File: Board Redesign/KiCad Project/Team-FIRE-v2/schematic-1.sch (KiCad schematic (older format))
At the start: 20 parts

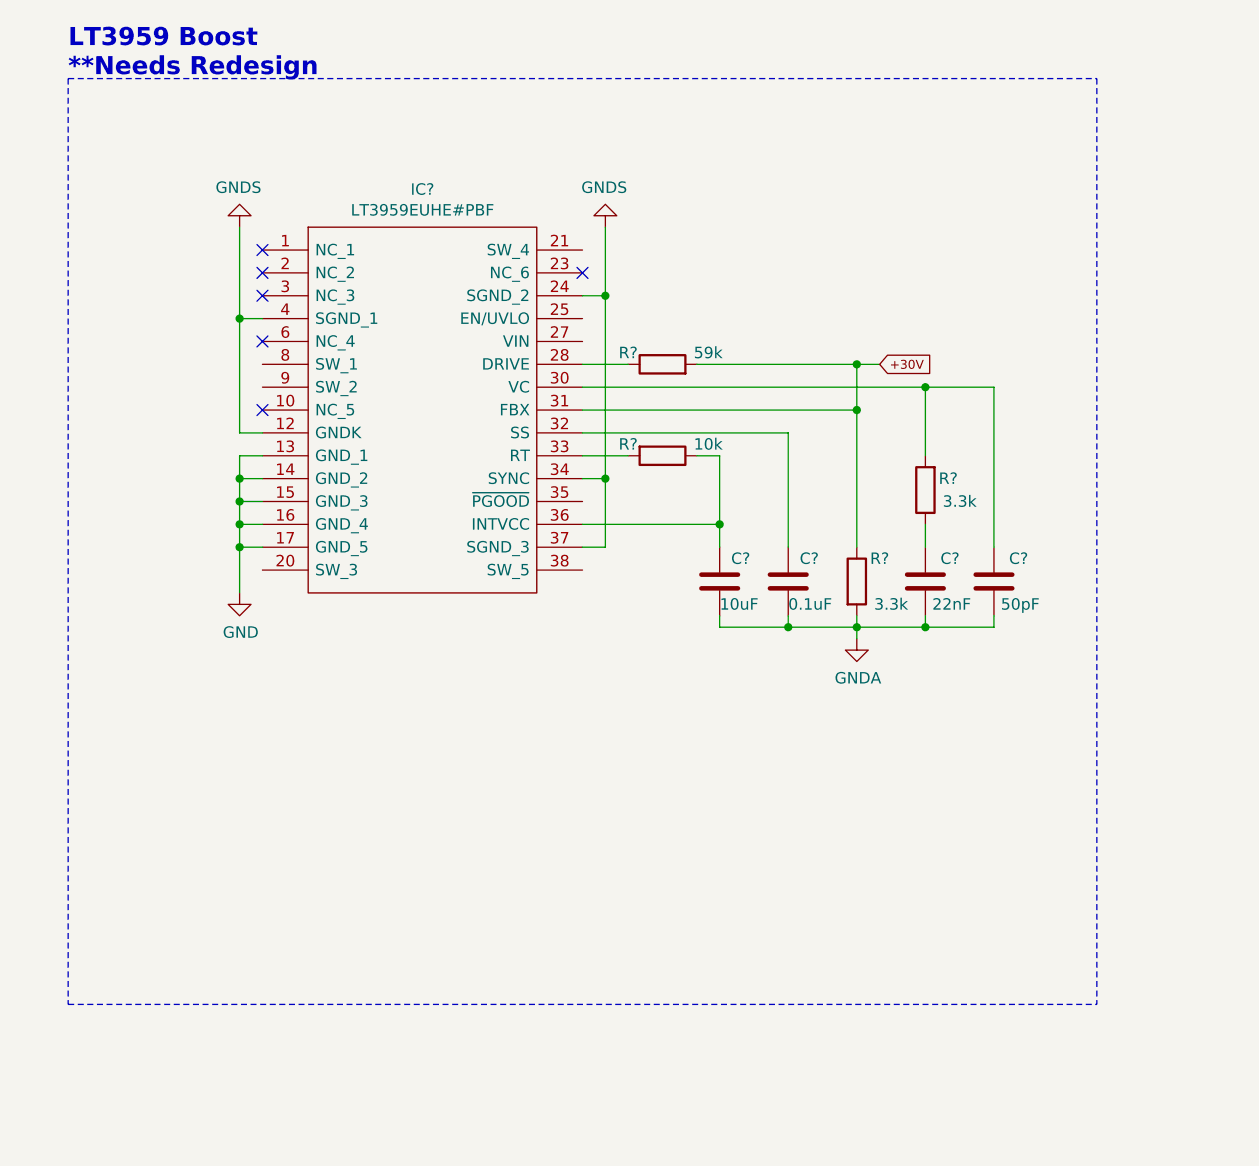
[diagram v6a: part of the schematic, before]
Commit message: Deleted Old Boost...
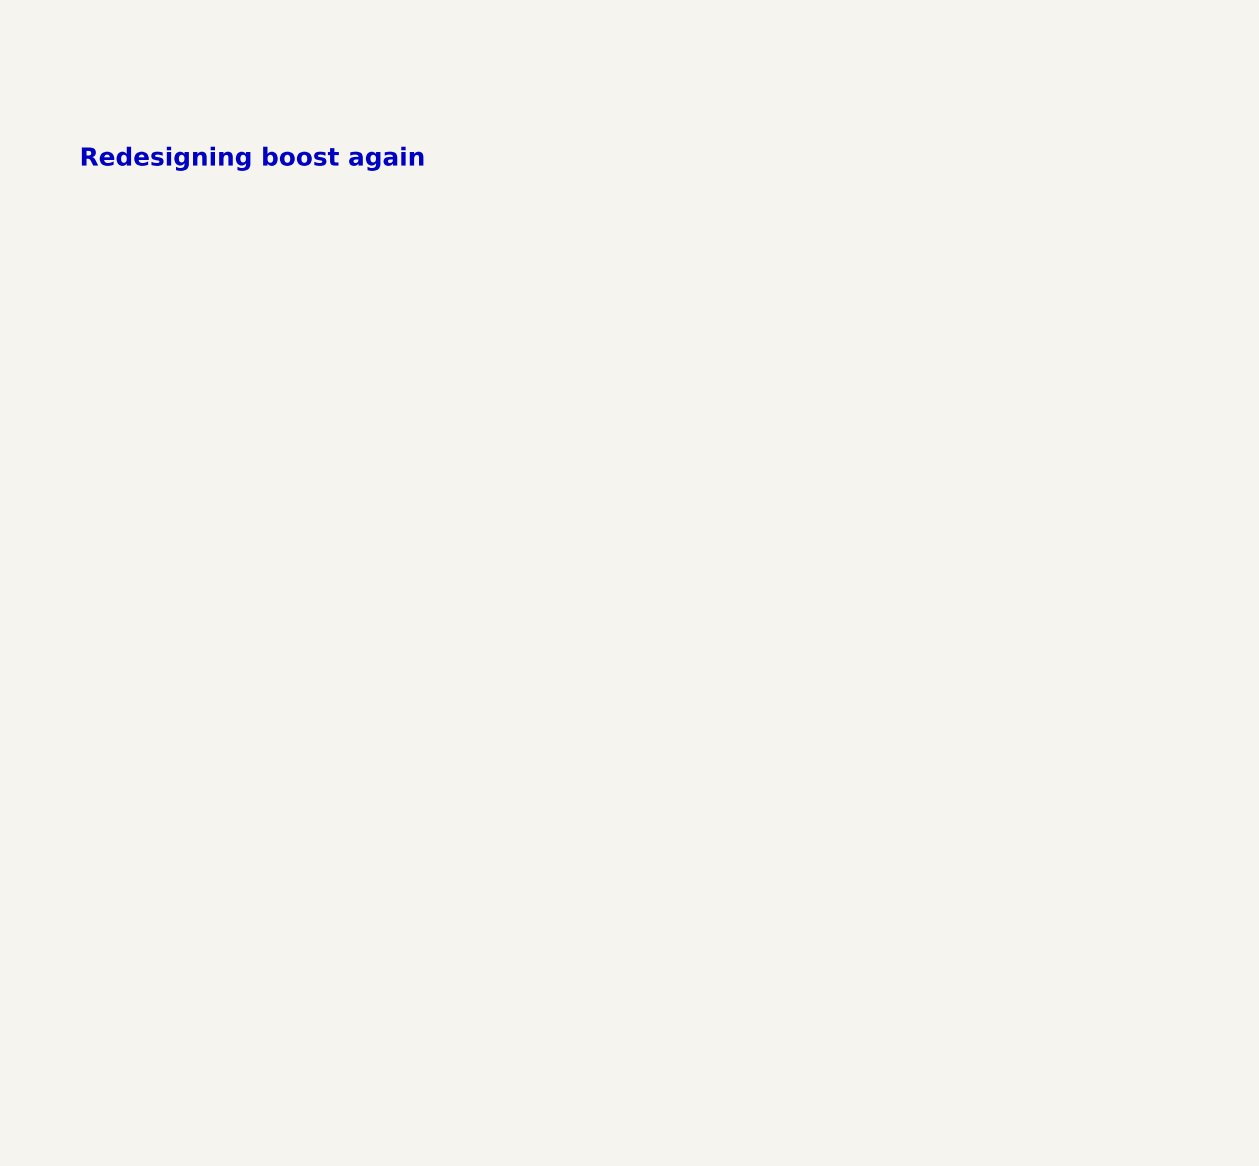
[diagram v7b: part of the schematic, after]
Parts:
- removed C?: 10uF, Capacitor_SMD:C_0603_1608Metric, symbol Device:C
- removed C?: 0.1uF, Capacitor_SMD:C_0603_1608Metric, symbol Device:C
- removed C?: 22nF, Capacitor_SMD:C_0603_1608Metric, symbol Device:C
- removed C?: 50pF, Capacitor_SMD:C_0603_1608Metric, symbol Device:C
- removed IC?: LT3959EUHE#PBF, Team-FIRE:LT3959EUHEPBF, symbol Team-FIRE:LT3959EUHE#PBF
- removed R?: 10k, Resistor_SMD:R_0603_1608Metric, symbol Device:R
- removed R? (x2): 3.3k, Resistor_SMD:R_0603_1608Metric, symbol Device:R
- removed R?: 59k, Resistor_SMD:R_0603_1608Metric, symbol Device:R
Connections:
- no-connect marks 17 -> 11
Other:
- note added: "Redesigning boost again"
- note removed: "LT3959 Boost\n**Needs Redesign"
